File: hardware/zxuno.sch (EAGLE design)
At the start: 103 parts, among them T1 BC846, U1 6SLX9TQG144, U2 FLASH-SPI-25XXSMD1, U4 AD724, U5 50MHz, U6 3.3V, U7 1.2V, Y1 3.58M, Y2 4.43M

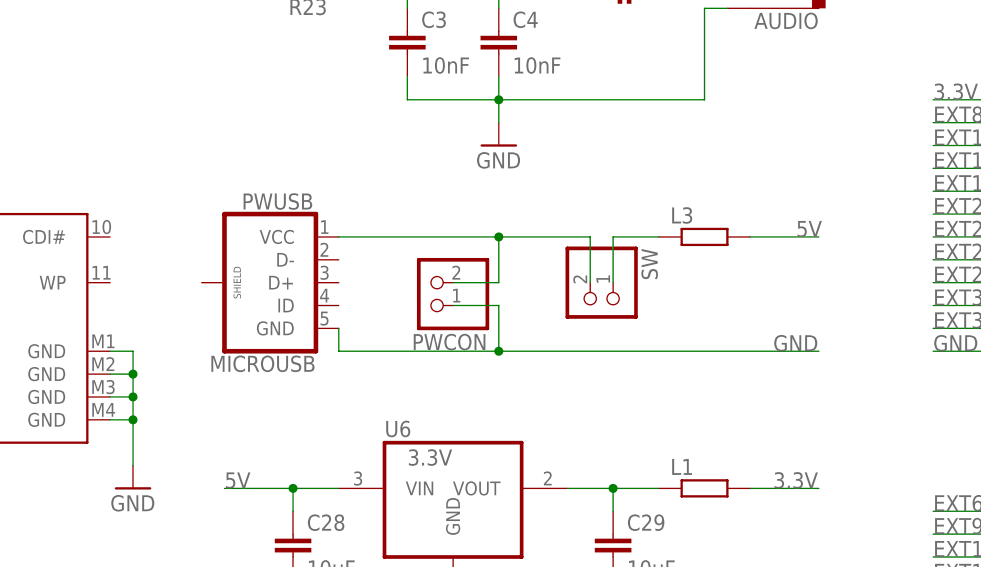
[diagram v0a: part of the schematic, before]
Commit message: Añado pines de datos al conector microUSB
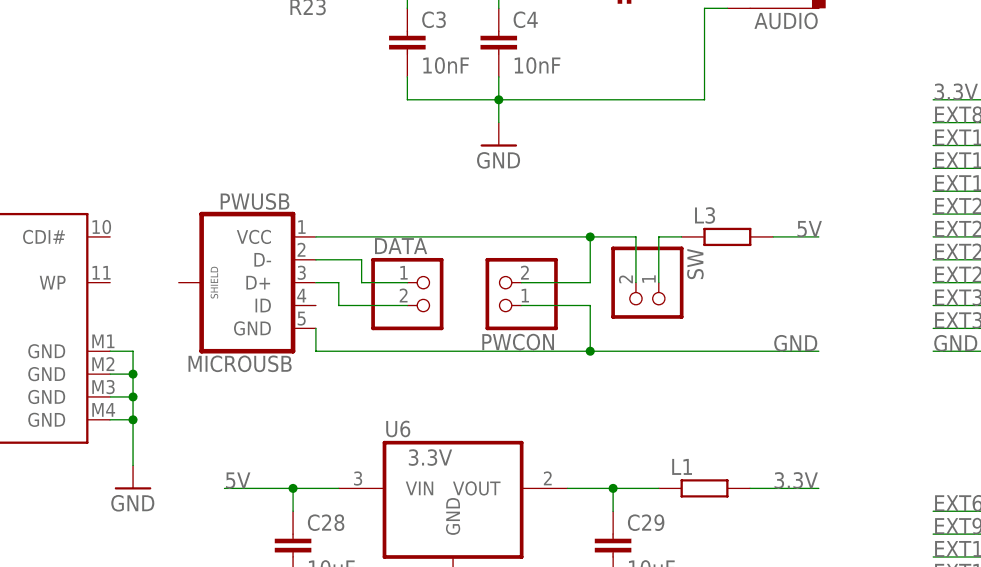
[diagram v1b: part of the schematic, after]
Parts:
- added DATA: (no value), pinhead:PINHD-1X2
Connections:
- new net N$16: DATA.1, PWUSB.D-
- new net N$29: DATA.2, PWUSB.D+
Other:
- moved on the sheet: L3, PWCON, PWUSB, SW
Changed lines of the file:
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@@
 <part name="J16" library="pinhead" deviceset="PINHD-2X2" device=""/>
 <part name="CVBS" library="uzebox" deviceset="RCA" device=""/>
+<part name="DATA" library="pinhead" deviceset="PINHD-1X2" device=""/>
 </parts>
 <sheets>
@@
 <instance part="R30" gate="G$1" x="121.92" y="5.08" rot="R270"/>
 <instance part="3.3V6" gate="VCC" x="121.92" y="17.78"/>
-<instance part="L3" gate="G$1" x="236.22" y="12.7"/>
+<instance part="L3" gate="G$1" x="238.76" y="12.7"/>
 <instance part="U6" gate="G$1" x="208.28" y="-15.24"/>
 <instance part="U7" gate="G$1" x="208.28" y="-40.64"/>
@@
 <instance part="JTAG" gate="-6" x="274.32" y="83.82"/>
 <instance part="RST" gate="G$1" x="119.38" y="68.58" rot="R270"/>
-<instance part="SW" gate="G$1" x="223.52" y="5.08" rot="R270"/>
-<instance part="PWCON" gate="G$1" x="205.74" y="7.62" rot="R180"/>
+<instance part="SW" gate="G$1" x="228.6" y="5.08" rot="R270"/>
+<instance part="PWCON" gate="G$1" x="213.36" y="7.62" rot="R180"/>
 <instance part="PS/2" gate="G$1" x="-25.4" y="-55.88"/>
 <instance part="U5" gate="G$1" x="0" y="81.28"/>
@@
 <instance part="D3" gate="G$1" x="195.58" y="-132.08" rot="R270"/>
 <instance part="H1" gate="G$1" x="-40.64" y="78.74"/>
-<instance part="PWUSB" gate="G$1" x="187.96" y="7.62" rot="MR0"/>
+<instance part="PWUSB" gate="G$1" x="185.42" y="7.62" rot="MR0"/>
 <instance part="SDCARD" gate="G$1" x="154.94" y="2.54"/>
 <instance part="GND19" gate="1" x="172.72" y="-15.24"/>
@@
 <instance part="J16" gate="A" x="157.48" y="-53.34"/>
 <instance part="CVBS" gate="G$1" x="276.86" y="-104.14" rot="MR0"/>
+<instance part="DATA" gate="G$1" x="205.74" y="5.08"/>
 </instances>
 <busses>
@@
 </segment>
 <segment>
-<wire x1="213.36" y1="0" x2="213.36" y2="5.08" width="0.1524" layer="91"/>
-<wire x1="213.36" y1="0" x2="248.92" y2="0" width="0.1524" layer="91"/>
-<junction x="213.36" y="0"/>
+<wire x1="223.52" y1="0" x2="223.52" y2="5.08" width="0.1524" layer="91"/>
+<wire x1="223.52" y1="0" x2="248.92" y2="0" width="0.1524" layer="91"/>
+<junction x="223.52" y="0"/>
 <label x="243.84" y="0" size="1.778" layer="95"/>
-<wire x1="195.58" y1="2.54" x2="195.58" y2="0" width="0.1524" layer="91"/>
-<wire x1="195.58" y1="0" x2="213.36" y2="0" width="0.1524" layer="91"/>
+<wire x1="193.04" y1="2.54" x2="193.04" y2="0" width="0.1524" layer="91"/>
+<wire x1="193.04" y1="0" x2="223.52" y2="0" width="0.1524" layer="91"/>
 <pinref part="PWCON" gate="G$1" pin="1"/>
-<wire x1="208.28" y1="5.08" x2="213.36" y2="5.08" width="0.1524" layer="91"/>
+<wire x1="215.9" y1="5.08" x2="223.52" y2="5.08" width="0.1524" layer="91"/>
 <pinref part="PWUSB" gate="G$1" pin="GND"/>
 </segment>
@@
 <net name="N$12" class="0">
 <segment>
-<wire x1="223.52" y1="12.7" x2="213.36" y2="12.7" width="0.1524" layer="91"/>
-<wire x1="213.36" y1="12.7" x2="195.58" y2="12.7" width="0.1524" layer="91"/>
-<wire x1="213.36" y1="7.62" x2="213.36" y2="12.7" width="0.1524" layer="91"/>
-<junction x="213.36" y="12.7"/>
+<wire x1="228.6" y1="12.7" x2="223.52" y2="12.7" width="0.1524" layer="91"/>
+<wire x1="223.52" y1="12.7" x2="193.04" y2="12.7" width="0.1524" layer="91"/>
+<wire x1="223.52" y1="7.62" x2="223.52" y2="12.7" width="0.1524" layer="91"/>
+<junction x="223.52" y="12.7"/>
 <pinref part="PWCON" gate="G$1" pin="2"/>
-<wire x1="208.28" y1="7.62" x2="213.36" y2="7.62" width="0.1524" layer="91"/>
+<wire x1="215.9" y1="7.62" x2="223.52" y2="7.62" width="0.1524" layer="91"/>
 <pinref part="SW" gate="G$1" pin="2"/>
-<wire x1="223.52" y1="7.62" x2="223.52" y2="12.7" width="0.1524" layer="91"/>
+<wire x1="228.6" y1="7.62" x2="228.6" y2="12.7" width="0.1524" layer="91"/>
 <pinref part="PWUSB" gate="G$1" pin="VCC"/>
 </segment>
@@
 <segment>
 <pinref part="L3" gate="G$1" pin="1"/>
-<wire x1="231.14" y1="12.7" x2="226.06" y2="12.7" width="0.1524" layer="91"/>
+<wire x1="233.68" y1="12.7" x2="231.14" y2="12.7" width="0.1524" layer="91"/>
 <pinref part="SW" gate="G$1" pin="1"/>
-<wire x1="226.06" y1="7.62" x2="226.06" y2="12.7" width="0.1524" layer="91"/>
+<wire x1="231.14" y1="7.62" x2="231.14" y2="12.7" width="0.1524" layer="91"/>
 </segment>
 </net>
@@
 <segment>
 <pinref part="L3" gate="G$1" pin="2"/>
-<wire x1="241.3" y1="12.7" x2="248.92" y2="12.7" width="0.1524" layer="91"/>
+<wire x1="243.84" y1="12.7" x2="248.92" y2="12.7" width="0.1524" layer="91"/>
 <label x="246.38" y="12.7" size="1.778" layer="95"/>
 </segment>
@@
 </segment>
 </net>
+<net name="N$16" class="0">
+<segment>
+<pinref part="PWUSB" gate="G$1" pin="D-"/>
+<wire x1="193.04" y1="10.16" x2="198.12" y2="10.16" width="0.1524" layer="91"/>
+<wire x1="198.12" y1="10.16" x2="198.12" y2="7.62" width="0.1524" layer="91"/>
+<pinref part="DATA" gate="G$1" pin="1"/>
+<wire x1="198.12" y1="7.62" x2="203.2" y2="7.62" width="0.1524" layer="91"/>
+</segment>
+</net>
+<net name="N$29" class="0">
+<segment>
+<pinref part="PWUSB" gate="G$1" pin="D+"/>
+<wire x1="193.04" y1="7.62" x2="195.58" y2="7.62" width="0.1524" layer="91"/>
+<wire x1="195.58" y1="7.62" x2="195.58" y2="5.08" width="0.1524" layer="91"/>
+<pinref part="DATA" gate="G$1" pin="2"/>
+<wire x1="195.58" y1="5.08" x2="203.2" y2="5.08" width="0.1524" layer="91"/>
+</segment>
+</net>

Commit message: Añado USB Blaster en plan addon
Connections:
- net N$16 renamed D-
- net N$29 renamed D+
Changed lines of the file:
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@@
 </segment>
 </net>
-<net name="N$16" class="0">
+<net name="D-" class="0">
 <segment>
 <pinref part="PWUSB" gate="G$1" pin="D-"/>
@@
 </segment>
 </net>
-<net name="N$29" class="0">
+<net name="D+" class="0">
 <segment>
 <pinref part="PWUSB" gate="G$1" pin="D+"/>

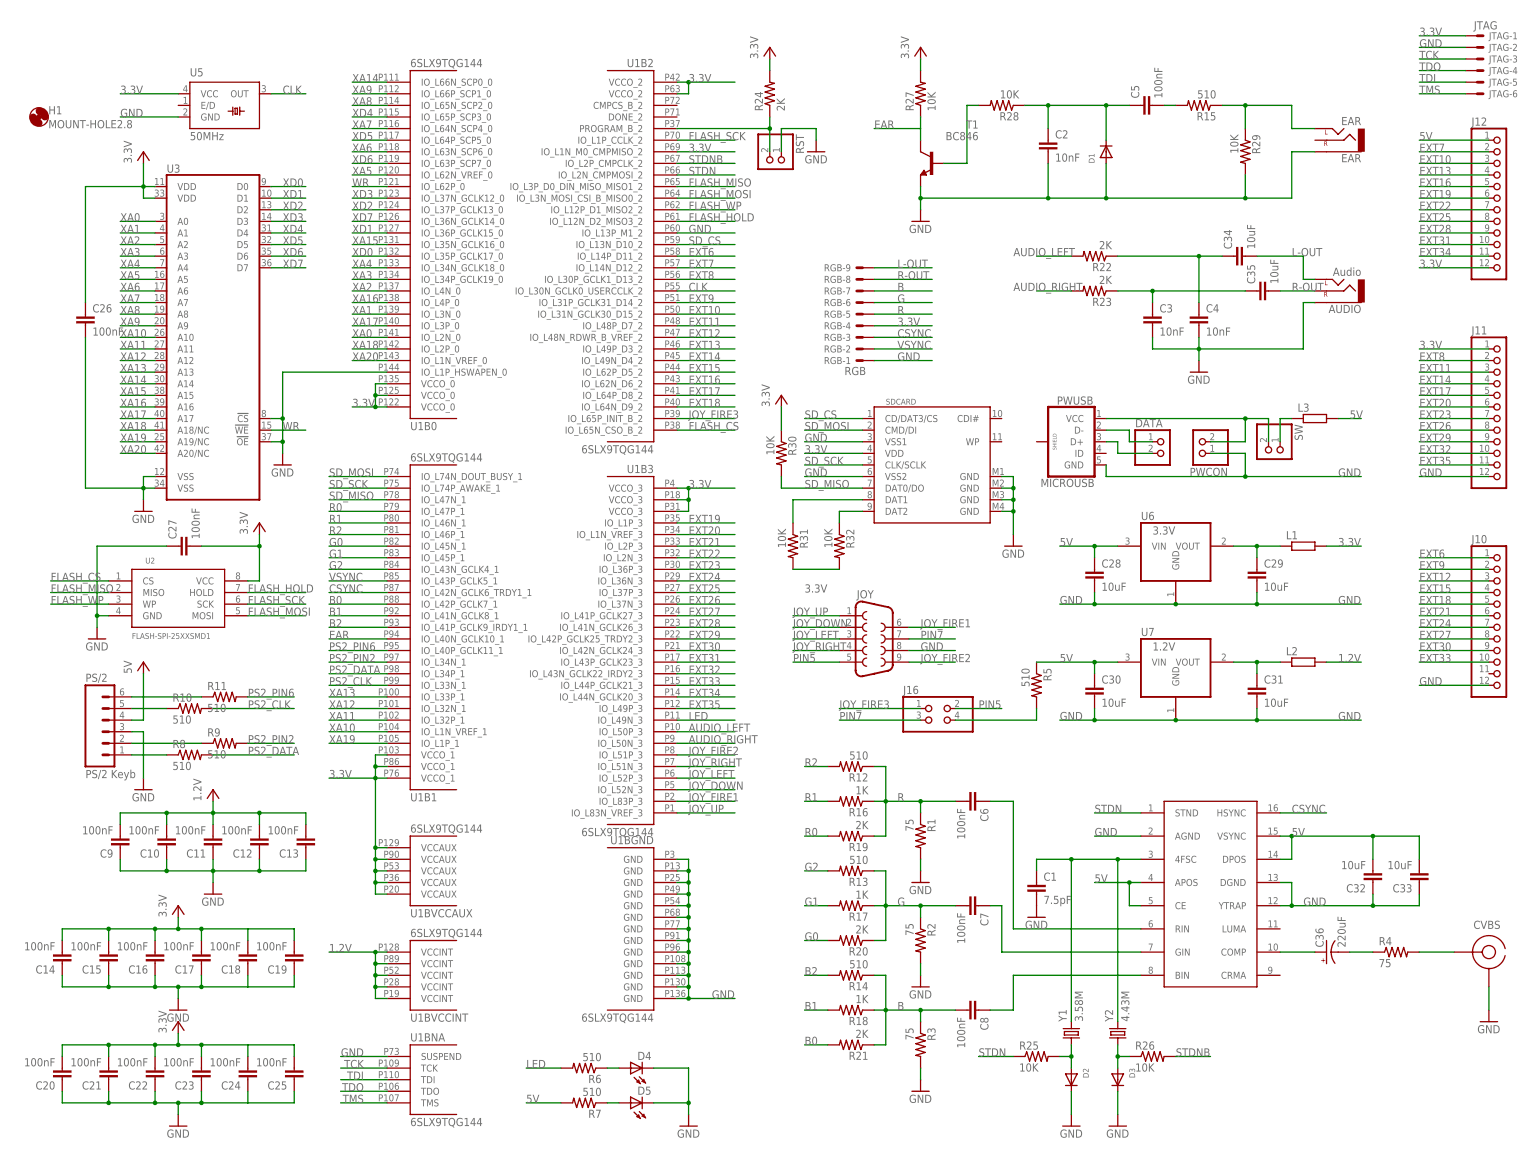
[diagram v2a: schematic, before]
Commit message: Quito pines de datos del microUSB, cambio JTAG a 2.54mm y pongo pines teclado con 5V
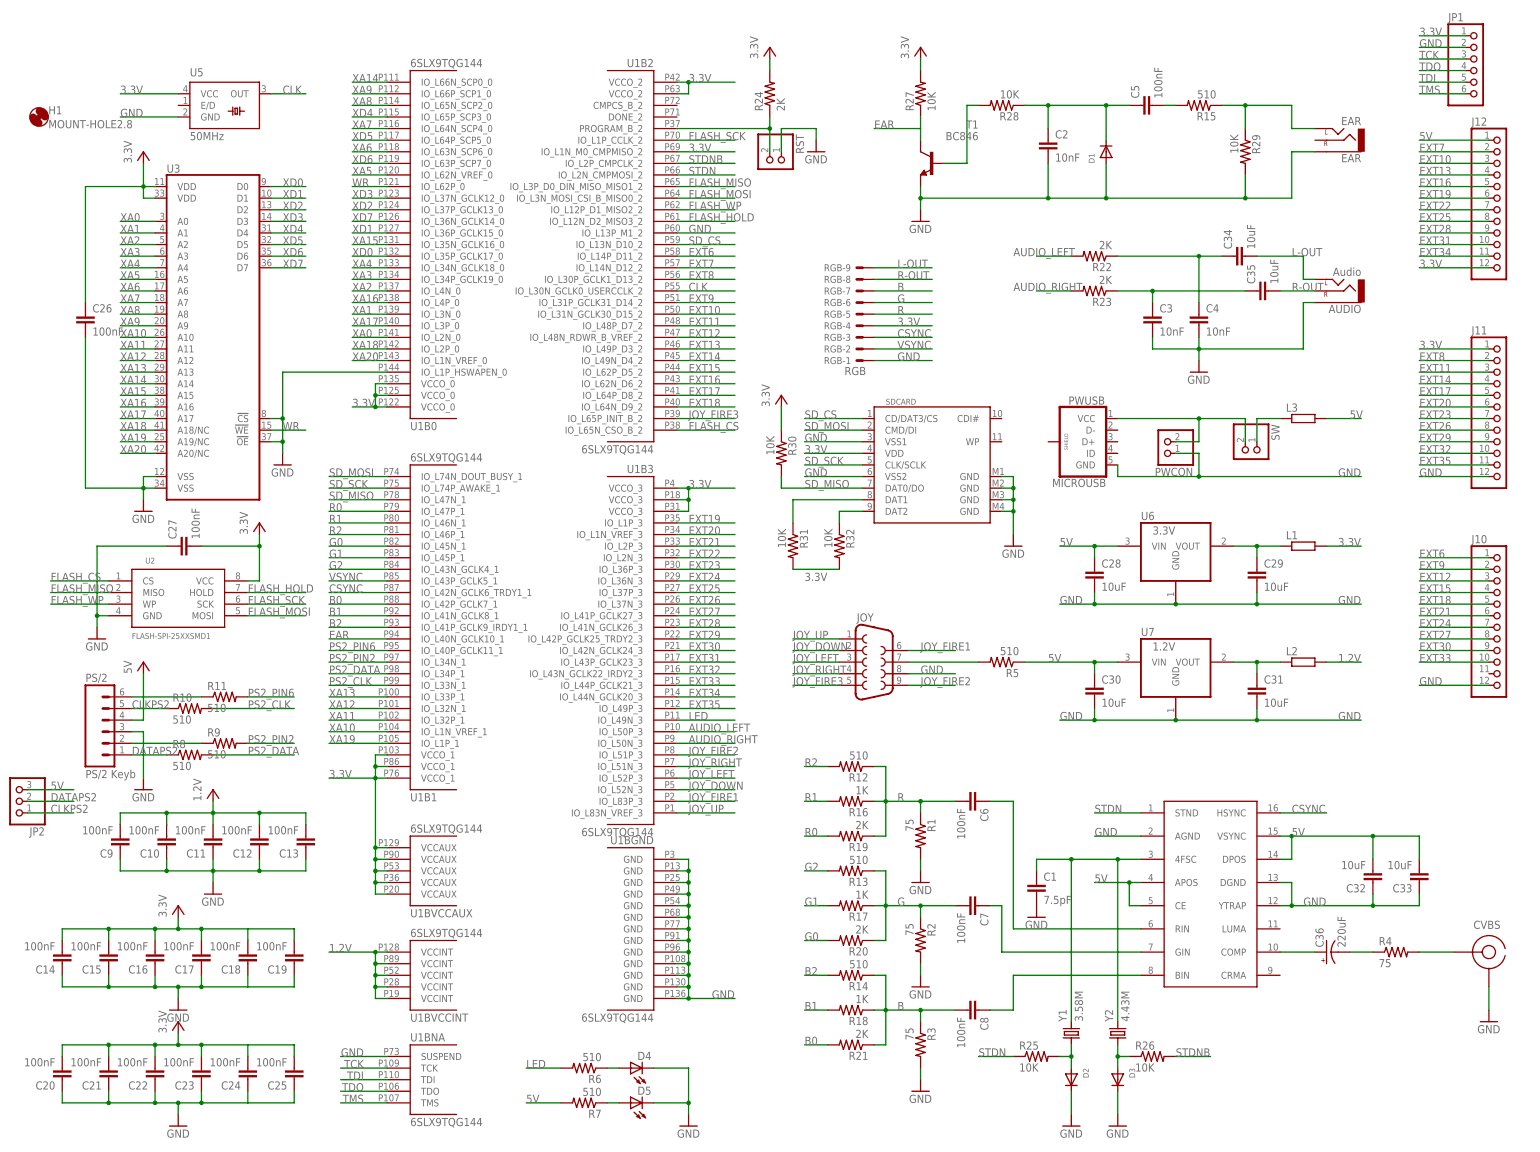
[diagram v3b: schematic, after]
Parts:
- removed DATA: (no value), pinhead:PINHD-1X2
- removed J16: (no value), pinhead:PINHD-2X2
- removed JTAG: JTAG, con-molex:53047-06
- added JP1: (no value), pinhead:PINHD-1X6
- added JP2: (no value), pinhead:PINHD-1X3
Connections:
- removed net D+: DATA.2, PWUSB.D+
- removed net D-: DATA.1, PWUSB.D-
- removed net N$2: PS/2.5, R10.1
- removed net N$4: PS/2.1, R8.1
- removed net PIN5: J16.2, JOY.5
- removed net PIN7: J16.3, JOY.7
- new net CLKPS2: JP2.1, PS/2.5, R10.1
- new net DATAPS2: JP2.2, PS/2.1, R8.1
- net 3.3V: now also JP1.1; no longer JTAG-1.S
- net 5V: now also JP2.3
- net GND: now also JP1.2; no longer JTAG-2.S
- net JOY_FIRE3: now also JOY.5; no longer J16.1
- net N$15: now also JOY.7; no longer J16.4
- net TCK: now also JP1.3; no longer JTAG-3.S
- net TDI: now also JP1.5; no longer JTAG-5.S
- net TDO: now also JP1.4; no longer JTAG-4.S
- net TMS: now also JP1.6; no longer JTAG-6.S
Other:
- moved on the sheet: JOY, L3, PWCON, PWUSB, R5, SW

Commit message: Últimos cambios, probablemente sea v4.2 definitiva
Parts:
- renumbered JP1 to JTAG, JP2 to KEYB
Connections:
- net CLKPS2: no longer KEYB.1
- net DATAPS2: no longer KEYB.2
- net PS2_CLK: now also KEYB.2
- net PS2_DATA: now also KEYB.1
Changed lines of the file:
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@@
 <part name="R32" library="rcl" deviceset="R-US_" device="M0805" value="10K"/>
 <part name="CVBS" library="uzebox" deviceset="RCA" device=""/>
-<part name="JP1" library="pinhead" deviceset="PINHD-1X6" device=""/>
-<part name="JP2" library="pinhead" deviceset="PINHD-1X3" device=""/>
+<part name="JTAG" library="pinhead" deviceset="PINHD-1X6" device=""/>
+<part name="KEYB" library="pinhead" deviceset="PINHD-1X3" device=""/>
 </parts>
 <sheets>
@@
 <instance part="R32" gate="G$1" x="134.62" y="-15.24" rot="R270"/>
 <instance part="CVBS" gate="G$1" x="276.86" y="-104.14" rot="MR0"/>
-<instance part="JP1" gate="A" x="274.32" y="88.9"/>
-<instance part="JP2" gate="A" x="-45.72" y="-71.12" rot="R180"/>
+<instance part="JTAG" gate="A" x="274.32" y="88.9"/>
+<instance part="KEYB" gate="A" x="-45.72" y="-71.12" rot="R180"/>
 </instances>
 <busses>
@@
 <wire x1="261.62" y1="96.52" x2="271.78" y2="96.52" width="0.1524" layer="91"/>
 <label x="261.62" y="96.52" size="1.778" layer="95"/>
-<pinref part="JP1" gate="A" pin="1"/>
+<pinref part="JTAG" gate="A" pin="1"/>
 </segment>
 <segment>
@@
 <wire x1="261.62" y1="93.98" x2="271.78" y2="93.98" width="0.1524" layer="91"/>
 <label x="261.62" y="93.98" size="1.778" layer="95"/>
-<pinref part="JP1" gate="A" pin="2"/>
+<pinref part="JTAG" gate="A" pin="2"/>
 </segment>
 </net>
@@
 <pinref part="U1" gate="B1" pin="IO_L34P_1"/>
 </segment>
+<segment>
+<pinref part="KEYB" gate="A" pin="1"/>
+<wire x1="-43.18" y1="-73.66" x2="-33.02" y2="-73.66" width="0.1524" layer="91"/>
+<label x="-38.1" y="-73.66" size="1.778" layer="95"/>
+</segment>
 </net>
 <net name="PS2_CLK" class="0">
@@
 <label x="22.86" y="-45.72" size="1.778" layer="95"/>
 <pinref part="U1" gate="B1" pin="IO_L33N_1"/>
+</segment>
+<segment>
+<pinref part="KEYB" gate="A" pin="2"/>
+<wire x1="-43.18" y1="-71.12" x2="-33.02" y2="-71.12" width="0.1524" layer="91"/>
+<label x="-38.1" y="-71.12" size="1.778" layer="95"/>
 </segment>
 </net>
@@
 <wire x1="261.62" y1="83.82" x2="271.78" y2="83.82" width="0.1524" layer="91"/>
 <label x="261.62" y="83.82" size="1.778" layer="95"/>
-<pinref part="JP1" gate="A" pin="6"/>
+<pinref part="JTAG" gate="A" pin="6"/>
 </segment>
 </net>
@@
 <wire x1="261.62" y1="91.44" x2="271.78" y2="91.44" width="0.1524" layer="91"/>
 <label x="261.62" y="91.44" size="1.778" layer="95"/>
-<pinref part="JP1" gate="A" pin="3"/>
+<pinref part="JTAG" gate="A" pin="3"/>
 </segment>
 </net>
@@
 <wire x1="261.62" y1="88.9" x2="271.78" y2="88.9" width="0.1524" layer="91"/>
 <label x="261.62" y="88.9" size="1.778" layer="95"/>
-<pinref part="JP1" gate="A" pin="4"/>
+<pinref part="JTAG" gate="A" pin="4"/>
 </segment>
 </net>
@@
 <wire x1="261.62" y1="86.36" x2="271.78" y2="86.36" width="0.1524" layer="91"/>
 <label x="261.62" y="86.36" size="1.778" layer="95"/>
-<pinref part="JP1" gate="A" pin="5"/>
+<pinref part="JTAG" gate="A" pin="5"/>
 </segment>
 </net>
@@
 </segment>
 <segment>
-<pinref part="JP2" gate="A" pin="3"/>
+<pinref part="KEYB" gate="A" pin="3"/>
 <wire x1="-43.18" y1="-68.58" x2="-33.02" y2="-68.58" width="0.1524" layer="91"/>
 <label x="-38.1" y="-68.58" size="1.778" layer="95"/>
@@
 <wire x1="-12.7" y1="-60.96" x2="-20.32" y2="-60.96" width="0.1524" layer="91"/>
 <pinref part="PS/2" gate="G$1" pin="1"/>
-<label x="-20.32" y="-60.96" size="1.778" layer="95"/>
-</segment>
-<segment>
-<pinref part="JP2" gate="A" pin="2"/>
-<wire x1="-43.18" y1="-71.12" x2="-33.02" y2="-71.12" width="0.1524" layer="91"/>
-<label x="-38.1" y="-71.12" size="1.778" layer="95"/>
 </segment>
 </net>
@@
 <wire x1="-12.7" y1="-50.8" x2="-20.32" y2="-50.8" width="0.1524" layer="91"/>
 <pinref part="PS/2" gate="G$1" pin="5"/>
-<label x="-20.32" y="-50.8" size="1.778" layer="95"/>
-</segment>
-<segment>
-<pinref part="JP2" gate="A" pin="1"/>
-<wire x1="-43.18" y1="-73.66" x2="-33.02" y2="-73.66" width="0.1524" layer="91"/>
-<label x="-38.1" y="-73.66" size="1.778" layer="95"/>
-</segment>
-</net>
+</segment>
+</net>

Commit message: Cambios sugeridos por McLeod
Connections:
- net CLKPS2: now also KEYB.1
- net DATAPS2: now also KEYB.2
- net PS2_CLK: no longer KEYB.2
- net PS2_DATA: no longer KEYB.1
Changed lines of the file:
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@@
 <pinref part="U1" gate="B1" pin="IO_L34P_1"/>
-</segment>
-<segment>
-<pinref part="KEYB" gate="A" pin="1"/>
-<wire x1="-43.18" y1="-73.66" x2="-33.02" y2="-73.66" width="0.1524" layer="91"/>
-<label x="-38.1" y="-73.66" size="1.778" layer="95"/>
 </segment>
 </net>
@@
 <label x="22.86" y="-45.72" size="1.778" layer="95"/>
 <pinref part="U1" gate="B1" pin="IO_L33N_1"/>
-</segment>
-<segment>
-<pinref part="KEYB" gate="A" pin="2"/>
-<wire x1="-43.18" y1="-71.12" x2="-33.02" y2="-71.12" width="0.1524" layer="91"/>
-<label x="-38.1" y="-71.12" size="1.778" layer="95"/>
 </segment>
 </net>
@@
 <wire x1="-12.7" y1="-60.96" x2="-20.32" y2="-60.96" width="0.1524" layer="91"/>
 <pinref part="PS/2" gate="G$1" pin="1"/>
+<label x="-20.32" y="-60.96" size="1.778" layer="95"/>
+</segment>
+<segment>
+<pinref part="KEYB" gate="A" pin="2"/>
+<wire x1="-43.18" y1="-71.12" x2="-33.02" y2="-71.12" width="0.1524" layer="91"/>
+<label x="-38.1" y="-71.12" size="1.778" layer="95"/>
 </segment>
 </net>
@@
 <wire x1="-12.7" y1="-50.8" x2="-20.32" y2="-50.8" width="0.1524" layer="91"/>
 <pinref part="PS/2" gate="G$1" pin="5"/>
-</segment>
-</net>
+<label x="-20.32" y="-50.8" size="1.778" layer="95"/>
+</segment>
+<segment>
+<pinref part="KEYB" gate="A" pin="1"/>
+<wire x1="-43.18" y1="-73.66" x2="-33.02" y2="-73.66" width="0.1524" layer="91"/>
+<label x="-38.1" y="-73.66" size="1.778" layer="95"/>
+</segment>
+</net>
